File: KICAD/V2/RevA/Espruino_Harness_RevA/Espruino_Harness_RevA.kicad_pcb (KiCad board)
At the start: 2 copper layers, 100 x 90 mm, 229 parts, among them J1001 OPERATING_MODE Selection, J201 EXTERNAL_ANALOG_STIMULUS_0_TO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, J301 GROVE_I2C, J302 MCP23017_GPIO, J401 MCP3008_ANALOGUE_BREAKOUT, J402 ADAFRUIT_MICROSD_BFF_5683, J501 DS18B20_SENSOR_A, J502 DS18B20_SENSOR_B, J503 2K2_DQ_4K7, J504 DS2413_MODULE, J701 UART_PEER_DIAGNOSTIC, J902 PIXEL_SHIFTER_6066, Q1001 DMN2024UQ-7, Q1101 AO3401A, Q1201 2N7002, Q1202 2N7002, Q1203 DMG2302UKQ-7, Q301 2N7002, Q302 2N7002, U1001 TPS2116DRL, U1002 TPS22917DBV, U1101 TPS2559-Q1, U1102 TXU0101DBVR, U1103 INA226, U1104 INA228, U1105 74LVC2G08, U1201 MCP23017-E/SO, U301 MCP23017-E/SO, U401 MCP3008, U601 TMUX1511, U602 TMUX1511, U603 TMUX1511, U604 TMUX1511, U605 TMUX1511, U606 TMUX1511, U607 TPS3808G30DBVR, U608 TPS3808G30DBVR, U609 TPS3808G30DBVR, U610 MCP23017-E/SO RCTRL0, U611 MCP23017-E/SO RCTRL1, U701 TMUX1511

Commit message: Verify TB07 UART crosslink baseline
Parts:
- added J702: UART_B_DIAGNOSTIC_NO_DRIVE, Connector_PinHeader_2.54mm:PinHeader_1x03_P2.54mm_Vertical, F.Cu at (99.1, 45.7)
- J701: value UART_PEER_DIAGNOSTIC -> UART_PEER; footprint Connector_PinHeader_2.54mm:PinHeader_2x03_P2.54mm_Vertical -> Connector_PinHeader_2.54mm:PinHeader_1x03_P2.54mm_Vertical
- moved J701 40.0 mm to (94.5, 45.7)
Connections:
- J701 pad 2: /TI_UART_B_TX -> /Standard_Test_Blocks/UART_PEER_TX
- J701 pad 3: /Standard_Test_Blocks/UART_PEER_TX -> TI_GND

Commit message: Verify TB09 addressable RGB baseline
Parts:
- moved J902 30.6 mm to (114.3, 124.5), turned to -90 degrees
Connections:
- J902 pad 1: /TEST_BLOCK_3V3 -> TI_GND
- J902 pad 2: TI_GND -> /TEST_BLOCK_3V3

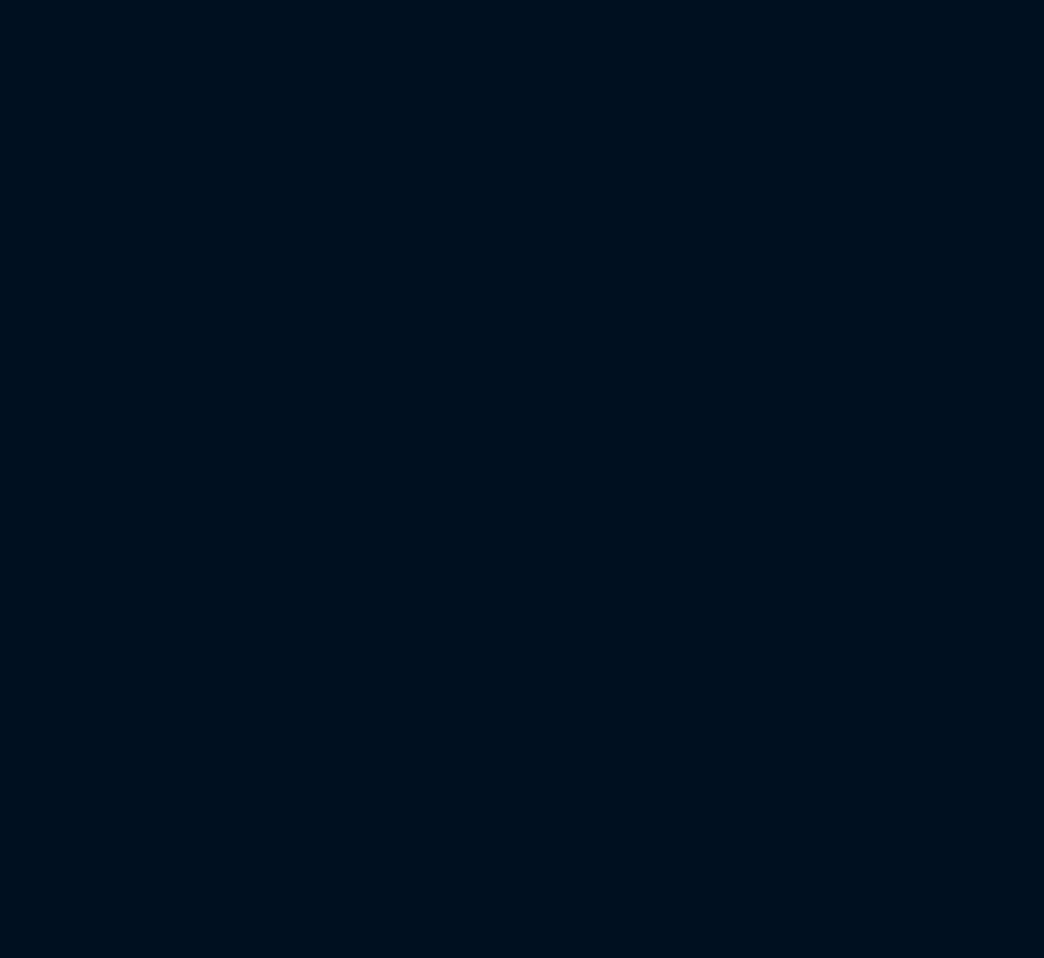
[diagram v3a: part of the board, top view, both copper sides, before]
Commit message: Implement Rev-A daughter-board foundations
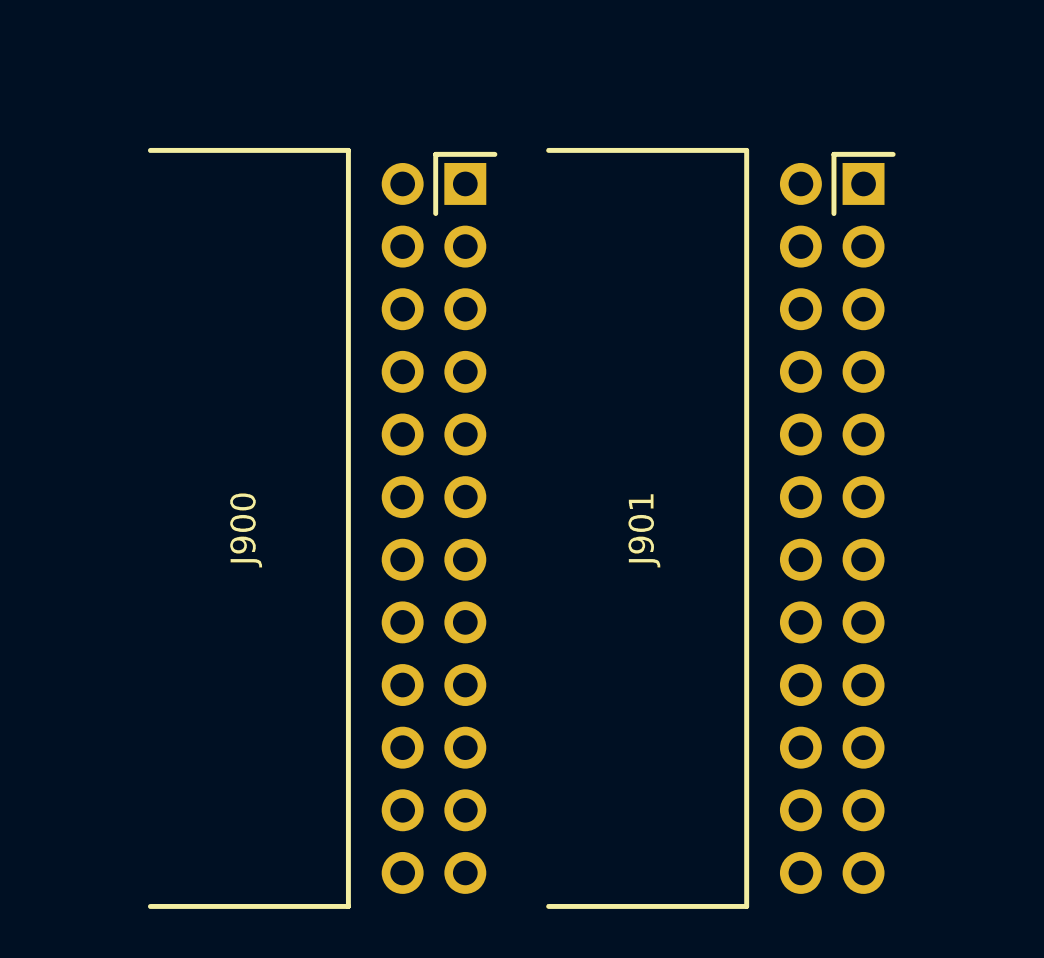
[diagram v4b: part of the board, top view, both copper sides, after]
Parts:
- added J900: TARGET INTERFACE CONNECTOR A, V2_Target_Interface:TargetInterface_2x12_P2.54mm_RA_Female_Adafruit1543_Harness, F.Cu at (42.3, 119.4)
- added J901: TARGET INTERFACE CONNECTOR B, V2_Target_Interface:TargetInterface_2x12_P2.54mm_RA_Female_Adafruit1543_Harness, F.Cu at (58.4, 119.4)
